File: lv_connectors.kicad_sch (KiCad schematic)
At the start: 4 parts, among them J3 Conn_01x02, J4 Conn_01x02, J6 Conn_01x02, J7 Conn_01x04

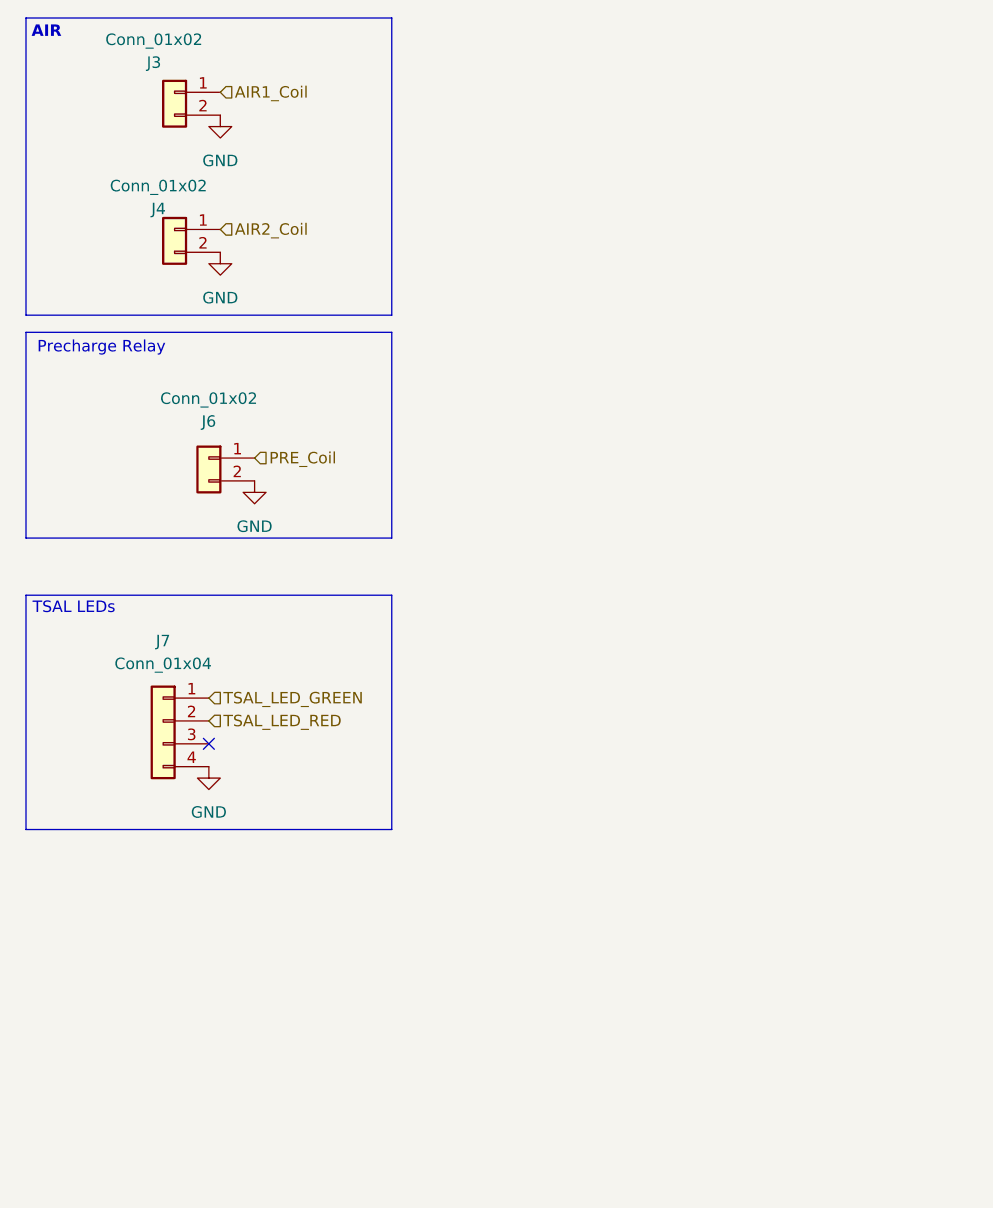
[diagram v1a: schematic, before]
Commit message: Changes to Pinout pending
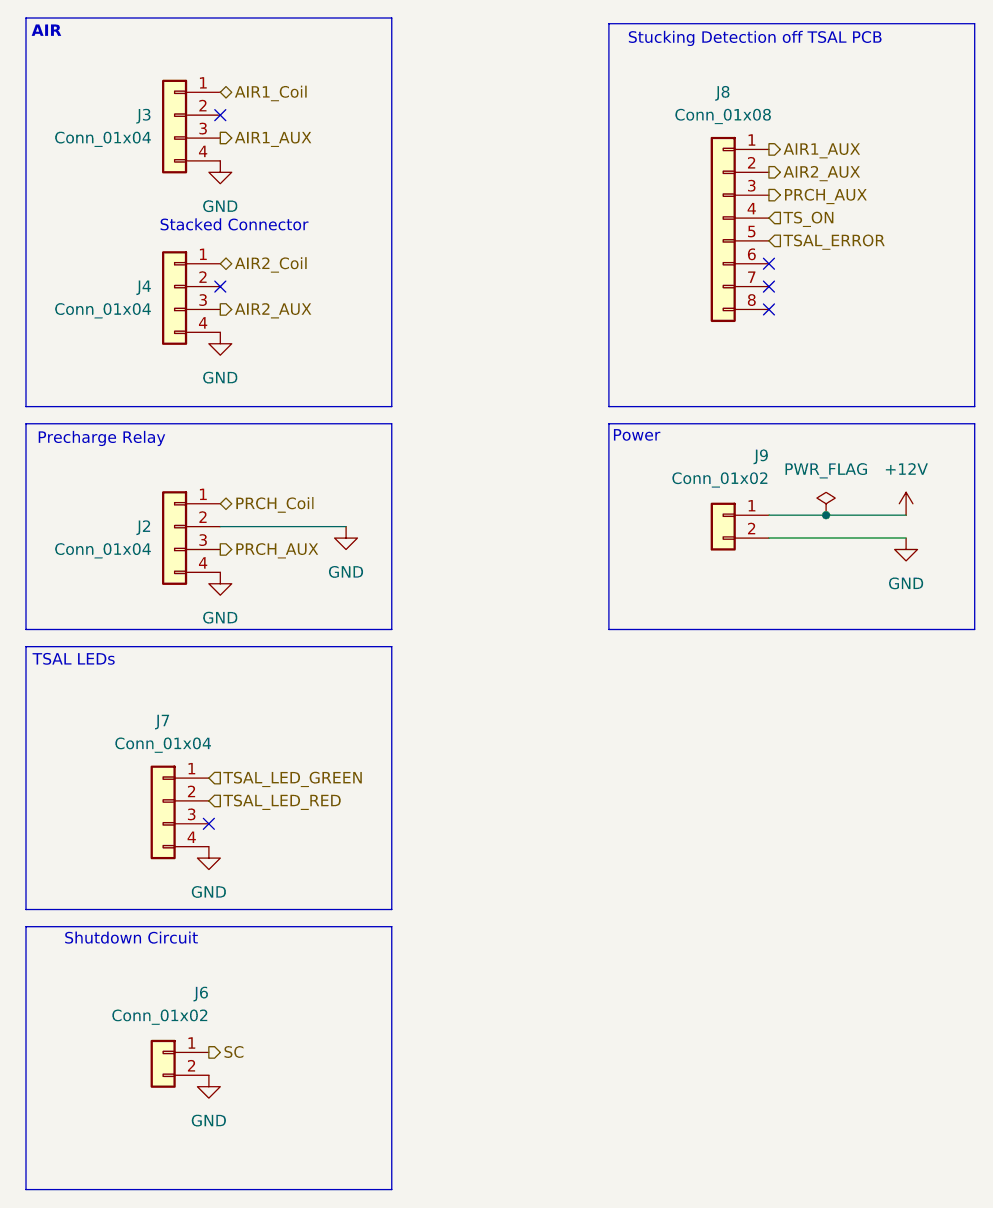
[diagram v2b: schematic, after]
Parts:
- removed J3, J4: Conn_01x02, wuerth_conn:66200211024, symbol Connector_Generic:Conn_01x02
- added J2, J3, J4: Conn_01x04, wuerth_conn:66200411022, symbol Connector_Generic:Conn_01x04
- added J8: Conn_01x08, symbol Connector_Generic:Conn_01x08
- added J9: Conn_01x02, wuerth_conn:66200211024, symbol Connector_Generic:Conn_01x02
- J6: Mouser 710-657002130101 -> (none); now left out of the parts list
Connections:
- net AIR1_Coil: now also J3.1 (Pin_1)
- net AIR2_Coil: now also J4.1 (Pin_1)
- net GND: now also J2.2 (Pin_2), J2.4 (Pin_4), J3.4 (Pin_4), J4.4 (Pin_4), J9.2 (Pin_2)
- net PRE_Coil renamed SC
- new net +12V: J9.1 (Pin_1)
- new net AIR1_AUX: J3.3 (Pin_3), J8.1 (Pin_1)
- new net AIR2_AUX: J4.3 (Pin_3), J8.2 (Pin_2)
- new net PRCH_AUX: J2.3 (Pin_3), J8.3 (Pin_3)
- new net PRCH_Coil: J2.1 (Pin_1)
- new net TSAL_ERROR: J8.5 (Pin_5)
- new net TS_ON: J8.4 (Pin_4)
- no-connect marks 1 -> 6
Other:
- note added: "Power"
- note added: "Shutdown Circuit"
- note added: "Stacked Connector"
- note added: "Stucking Detection off TSAL PCB"
- moved on the sheet: J7

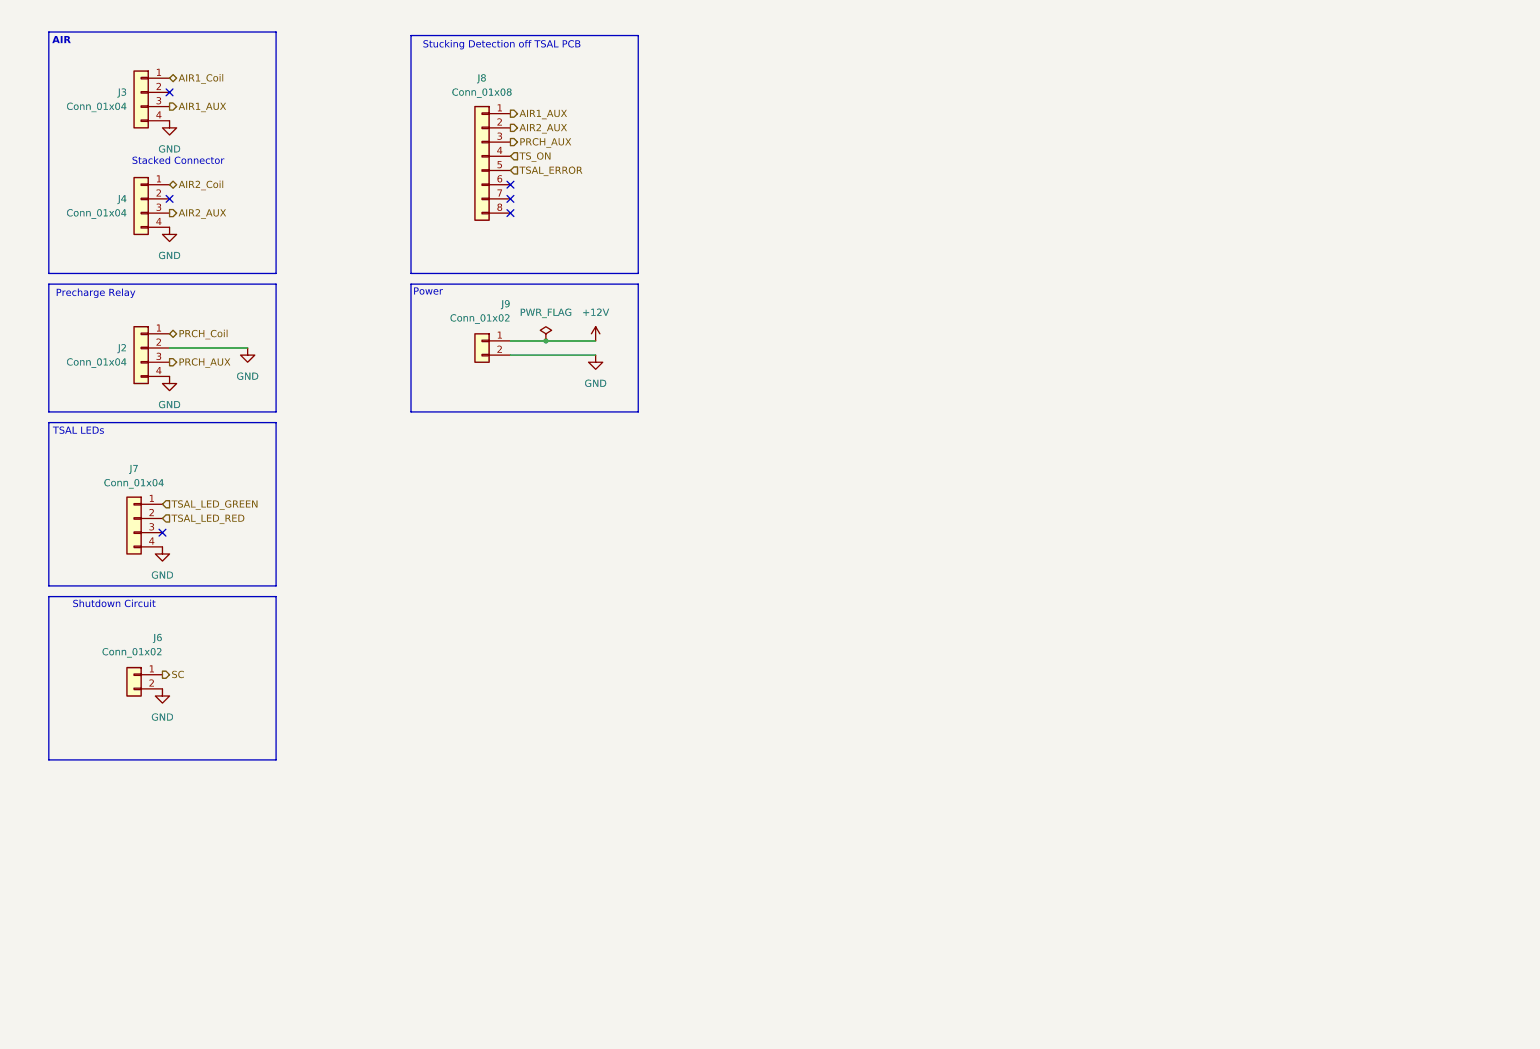
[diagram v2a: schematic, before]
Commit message: Checked Rules. Looks good. Need to fix AIR Aux detection. Need to Fix Coil Activation. Need to add SCS Failure Output and SCS Failure Inhibiter
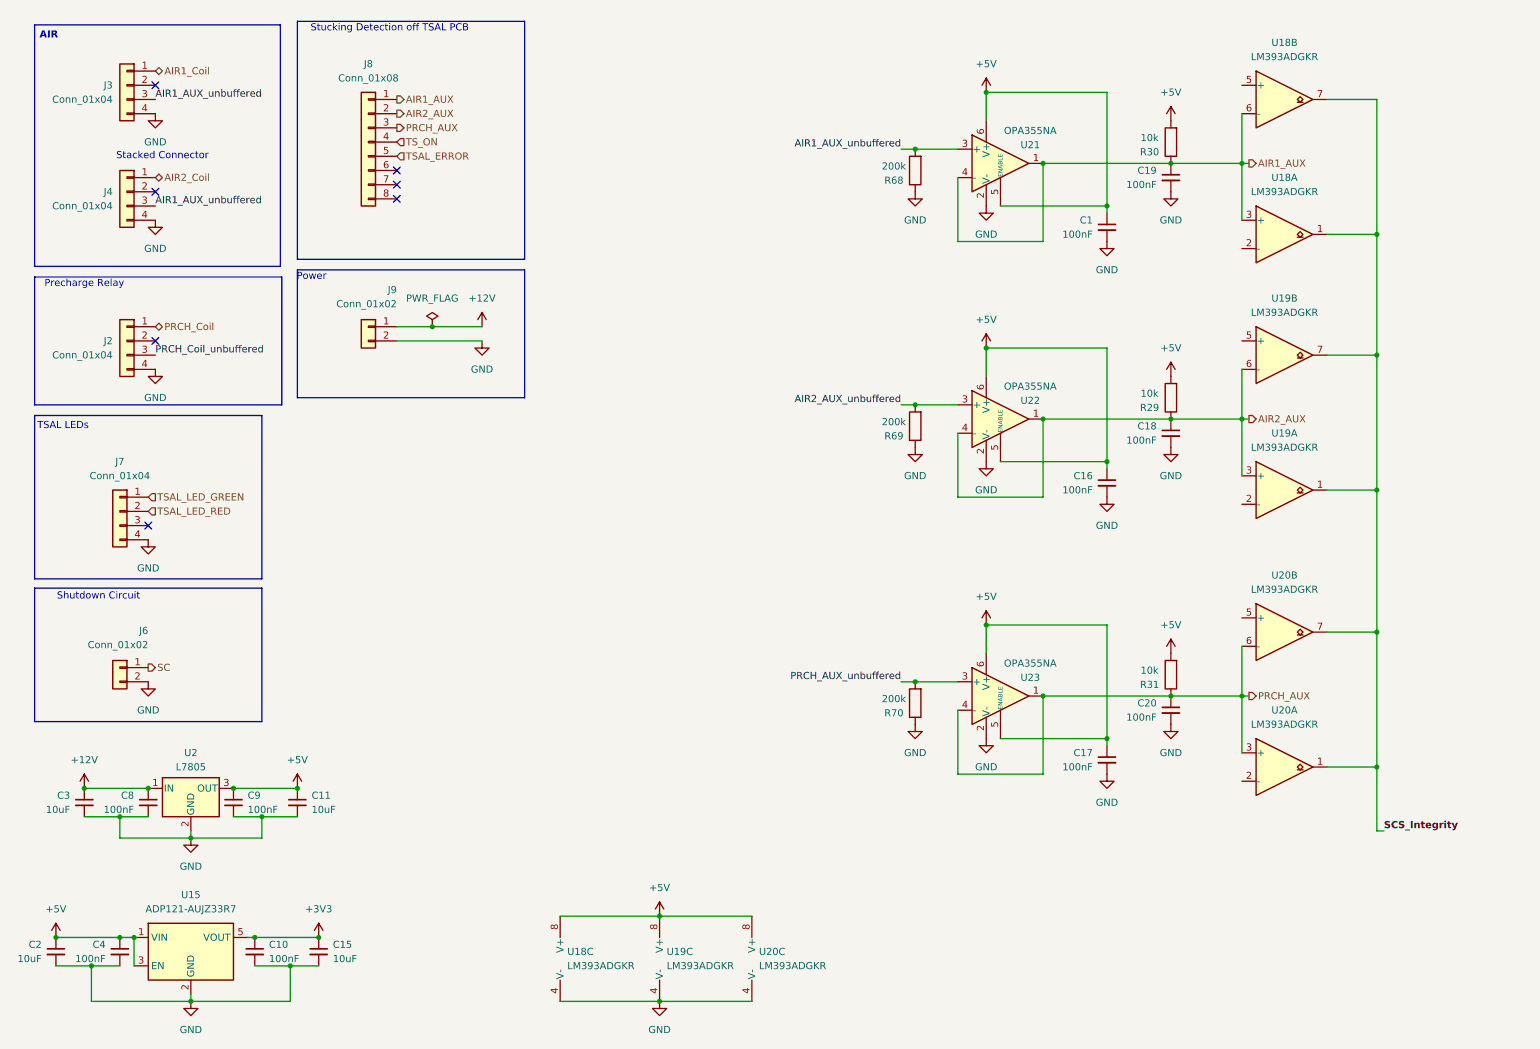
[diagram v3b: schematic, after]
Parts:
- added C1, C10, C16, C17, C18, C19, C20, C4, C8, C9: 100nF, Capacitor_SMD:C_0603_1608Metric, symbol Device:C_Small
- added C11, C15, C2, C3: 10uF, Capacitor_SMD:C_0603_1608Metric, symbol Device:C_Small
- added R29, R30, R31: 10k, Resistor_SMD:R_0603_1608Metric, symbol Device:R
- added R68, R69, R70: 200k, Resistor_SMD:R_0603_1608Metric, symbol Device:R
- added U15: ADP121-AUJZ33R7, Package_TO_SOT_SMD:TSOT-23-5, symbol Regulator_Linear:ADP7142AUJZ-3.3
- added U18, U19, U20: LM393ADGKR, Package_SO:VSSOP-8_3x3mm_P0.65mm, symbol Comparator:LM393
- added U2: L7805, Package_TO_SOT_SMD:TO-252-2, symbol Regulator_Linear:L7805
- added U21, U22, U23: OPA355NA, Package_TO_SOT_SMD:SOT-23-6, symbol Amplifier_Operational:OPA355NA
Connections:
- net +12V: now also C3.1, C8.1, U2.1 (IN)
- net AIR1_AUX: now also C19.1, R30.1, U18.3 (+), U18.6 (-), U21.1, U21.4 (-); no longer J3.3 (Pin_3)
- net AIR2_AUX: now also C18.1, R29.1, U19.3 (+), U19.6 (-), U22.1, U22.4 (-); no longer J4.3 (Pin_3)
- net GND: now also C1.2, C10.2, C11.2, C15.2, C16.2, C17.2, C18.2, C19.2, C2.2, C20.2, C3.2, C4.2, C8.2, C9.2, R68.1, R69.1, R70.1, U15.2 (GND), U18.4 (V-), U19.4 (V-), U2.2 (GND), U20.4 (V-), U21.2 (V-), U22.2 (V-), U23.2 (V-); no longer J2.2 (Pin_2)
- net PRCH_AUX: now also C20.1, R31.1, U20.3 (+), U20.6 (-), U23.1, U23.4 (-); no longer J2.3 (Pin_3)
- new net +3V3: C10.1, C15.1, U15.5 (VOUT)
- new net +5V: C1.1, C11.1, C16.1, C17.1, C2.1, C4.1, C9.1, R29.2, R30.2, R31.2, U15.1 (VIN), U15.3 (EN), U18.8 (V+), U19.8 (V+), U2.3 (OUT), U20.8 (V+), U21.5 (ENABLE), U21.6 (V+), U22.5 (ENABLE), U22.6 (V+), U23.5 (ENABLE), U23.6 (V+)
- new net AIR1_AUX_unbuffered: J3.3 (Pin_3), J4.3 (Pin_3), R68.2, U21.3 (+)
- new net AIR2_AUX_unbuffered: R69.2, U22.3 (+)
- new net PRCH_AUX_unbuffered: R70.2, U23.3 (+)
- new net PRCH_Coil_unbuffered: J2.3 (Pin_3)
- new net SCS_Integrity: U18.1, U18.7, U19.1, U19.7, U20.1, U20.7
- no-connect marks 6 -> 7
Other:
- moved on the sheet: J2, J3, J4, J6, J7, J8, J9

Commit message: Added new Subsheet
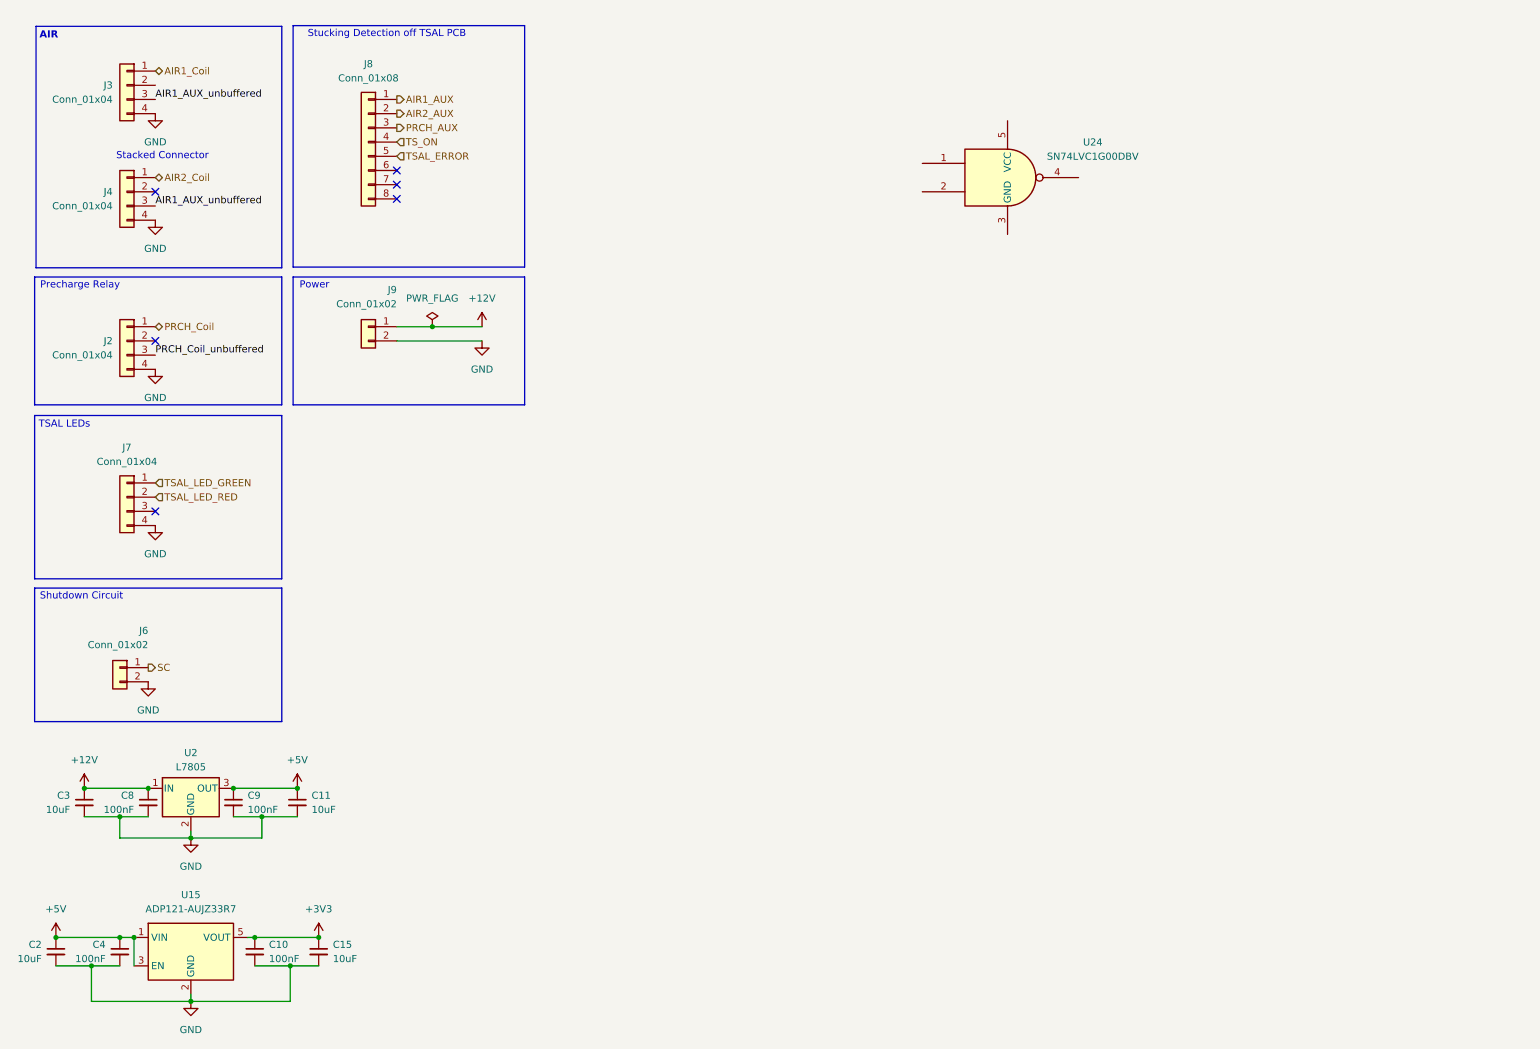
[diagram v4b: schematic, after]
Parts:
- removed C1, C16, C17, C18, C19, C20: 100nF, Capacitor_SMD:C_0603_1608Metric, symbol Device:C_Small
- removed R29, R30, R31: 10k, Resistor_SMD:R_0603_1608Metric, symbol Device:R
- removed R68, R69, R70: 200k, Resistor_SMD:R_0603_1608Metric, symbol Device:R
- removed U18, U19, U20: LM393ADGKR, Package_SO:VSSOP-8_3x3mm_P0.65mm, symbol Comparator:LM393
- removed U21, U22, U23: OPA355NA, Package_TO_SOT_SMD:SOT-23-6, symbol Amplifier_Operational:OPA355NA
- added U24: SN74LVC1G00DBV, Package_TO_SOT_SMD:SOT-23-5, symbol 74xGxx:SN74LVC1G00DBV
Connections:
- no-connect marks 7 -> 6
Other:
- moved on the sheet: J7
